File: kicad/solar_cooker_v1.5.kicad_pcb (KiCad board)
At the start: 2 copper layers, 160.5 x 77.2 mm, 20 parts, among them J1 Pt100, J2 microSD, J3 clock_module, J4 Pt100, J5 BME680, J6 GPS, J7 Pt100, J8 display, U1 anemometer, U2 AM2315C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

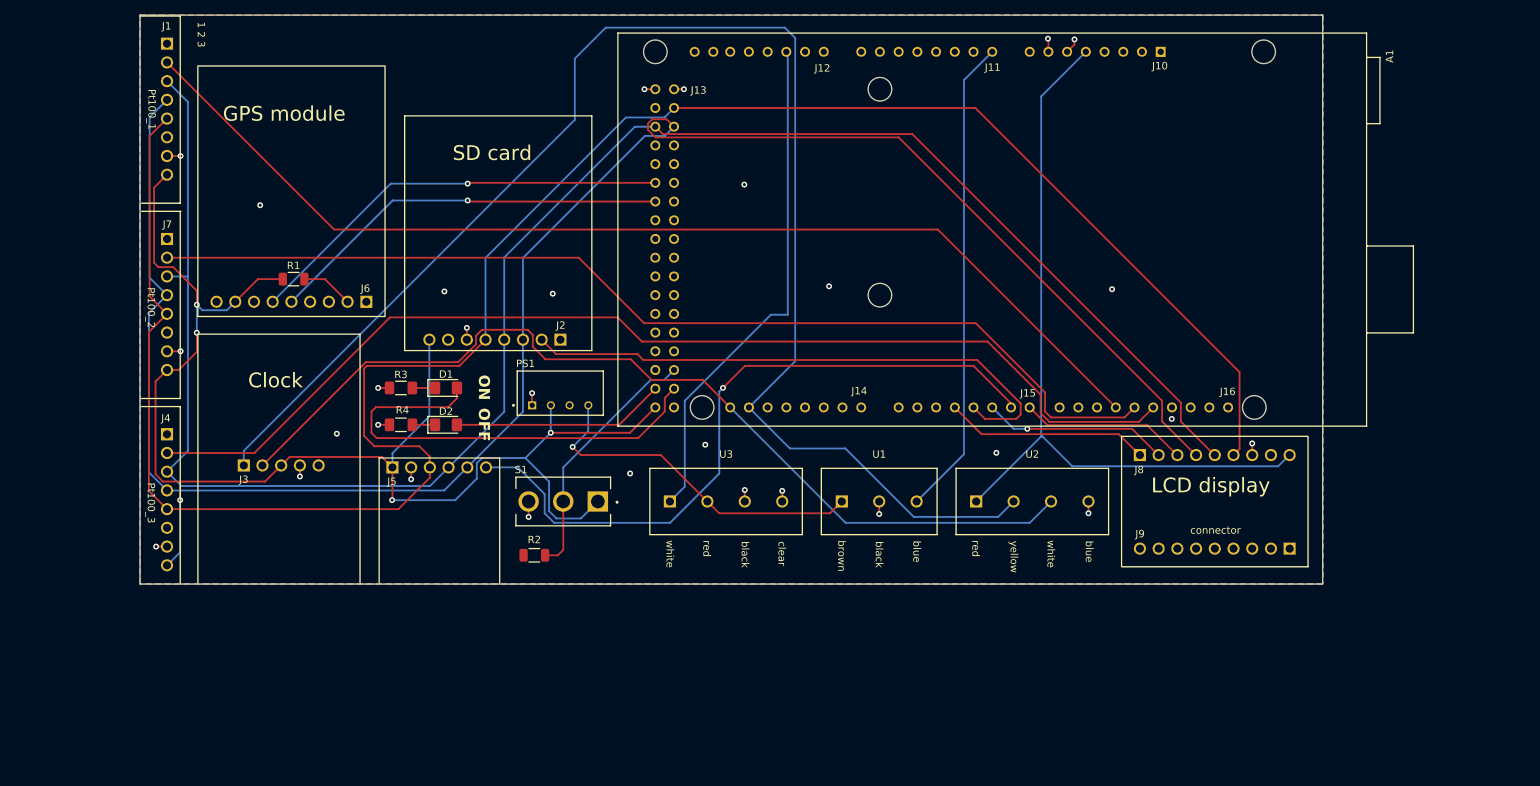
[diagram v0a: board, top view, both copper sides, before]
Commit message: fixed GPS and clock module in kicad
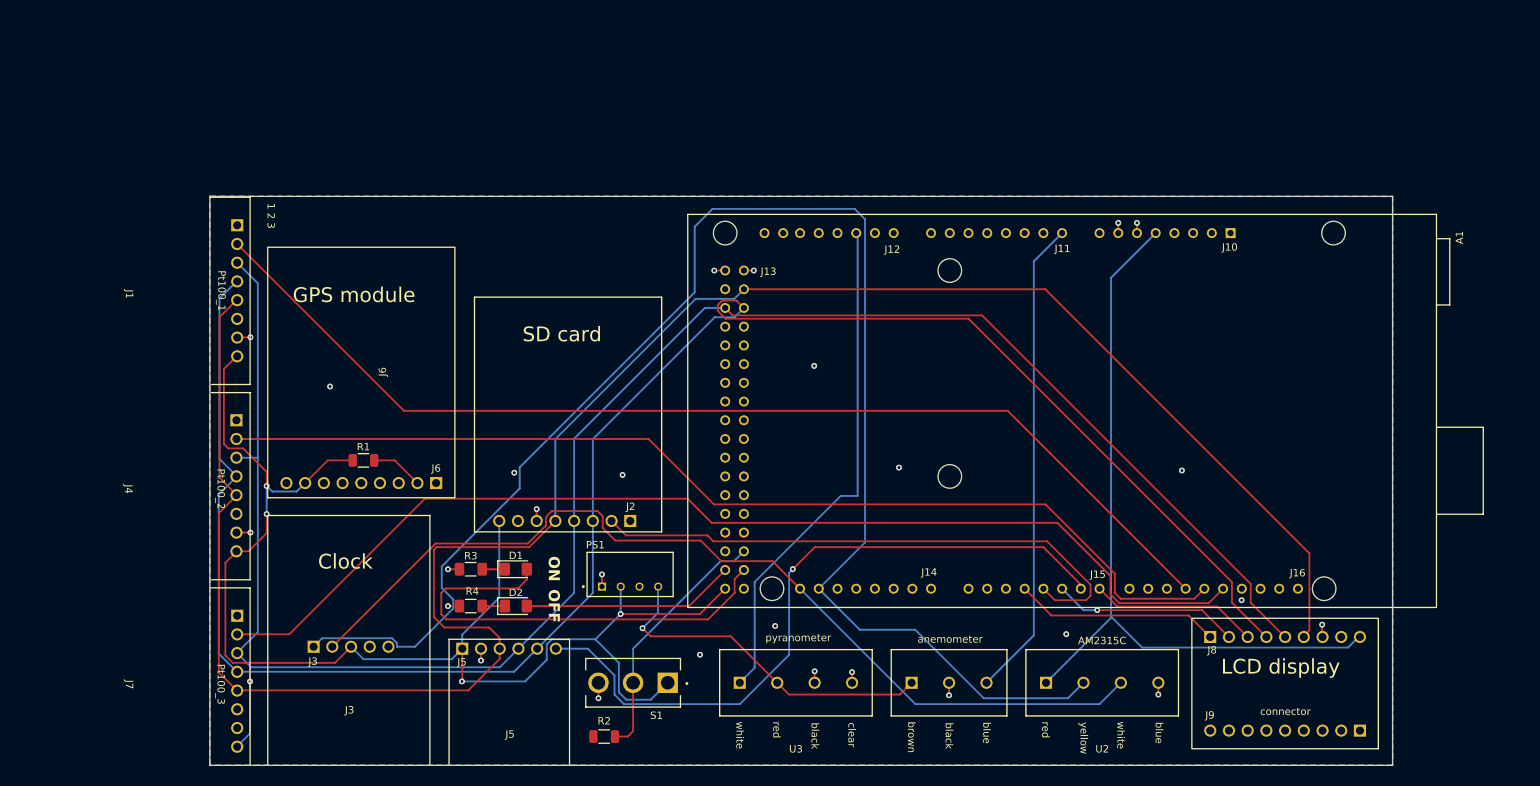
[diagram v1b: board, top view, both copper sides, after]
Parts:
- D1: value LED -> LED_GREEN
- D2: value LED -> LED_RED
- J1, J4, J7: footprint custom_components:Pt100 -> custom_components:PT100
- R1, R2: value R_Small -> 10k
- R3, R4: value R_Small -> 150
- moved J7 52.0 mm to (57.8, 145.8)
- moved J8 26.5 mm to (216.0, 144.9)
- moved J1 26.4 mm to (57.8, 92.9)
- moved R2 26.4 mm to (123.6, 153.3)
- moved D2 26.4 mm to (111.6, 135.6)
- moved J2 26.4 mm to (118.7, 107.7)
- moved J3 26.4 mm to (89.3, 141.0)
- moved J6 26.4 mm to (90.6, 103.9)
- moved PS1 26.4 mm to (127.1, 131.3)
- moved R4 26.4 mm to (105.5, 135.6)
- moved A1 26.4 mm to (185.7, 109.1)
- moved U1 26.4 mm to (170.4, 146.0)
- moved U2 26.4 mm to (191.2, 146.0)
- moved U3 26.4 mm to (149.6, 146.0)
- moved D1 26.4 mm to (111.6, 130.6)
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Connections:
- A1 pad 18: unconnected-(A1-Pad18) -> /TX1
- A1 pad 19: unconnected-(A1-Pad19) -> /RX1
- J4 pad 2: /D13 -> /D12
- J6 pad 5: /D43 -> /RX1
- J6 pad 6: /D45 -> /TX1
- J7 pad 2: /D12 -> /D13
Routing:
- net /D45: track 58.6 -> 0.00 mm, vias 1 -> 0
- net /D43: track 55.1 -> 0.00 mm, vias 1 -> 0
- net /SDA: track 201.7 -> 209.4 mm
- net GND: track 31.3 -> 27.2 mm, vias 30 -> 27

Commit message: footprints update
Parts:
- moved U1 21.9 mm to (192.3, 146.0)
- moved U2 19.8 mm to (171.4, 146.0)
- moved J2 9.61 mm to (117.9, 98.2)
- moved D2 8.34 mm to (115.3, 128.1)
- moved R4 7.93 mm to (107.8, 128.0), turned to 0 degrees
- moved D1 6.93 mm to (115.3, 124.7)
- moved R1 6.83 mm to (90.3, 109.0), turned to 0 degrees
- moved R3 6.31 mm to (107.8, 124.7), turned to 0 degrees
- moved A1 5.64 mm to (191.4, 108.9)
- moved R2 5.16 mm to (128.7, 154.1), turned to 180 degrees
- moved J6 4.97 mm to (90.2, 99.0)
- moved PS1 4.95 mm to (128.0, 126.4)
- moved J5 3.77 mm to (109.7, 145.8)
- moved J3 3.65 mm to (88.8, 137.4)
- moved U3 1.67 mm to (148.0, 146.0)
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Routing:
- net +5V: track 298.2 -> 0.00 mm, vias 5 -> 0
- net /SCK: track 282.9 -> 0.00 mm
- net /MISO: track 257.8 -> 0.00 mm
- net /MOSI: track 253.5 -> 0.00 mm
- net /SDA: track 209.4 -> 0.00 mm
- net /D13: track 149.6 -> 0.00 mm
- net /D11: track 148.1 -> 0.00 mm
- net /D12: track 142.4 -> 0.00 mm
- net /SCL: track 128.3 -> 0.00 mm
- net /D6: track 93.9 -> 0.00 mm, vias 1 -> 0
- net /D4: track 77.4 -> 0.00 mm
- net /A10: track 69.1 -> 0.00 mm
- net /A0: track 65.3 -> 0.00 mm
- net /D22: track 61.9 -> 0.00 mm
- net +9V: track 47.4 -> 0.00 mm, vias 1 -> 0
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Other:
- board text removed: "1 2 3"
- board text removed: "Clock"
- board text removed: "GPS module"
- board text removed: "J10"
- board text removed: "J11"
- board text removed: "J12"
- board text removed: "J13"
- board text removed: "J14"
- board text removed: "J15"
- board text removed: "J16"
- board text removed: "J9"
- board text removed: "LCD display"
- board text removed: "OFF"
- board text removed: "ON"
- board text removed: "Pt100_1"
- board text removed: "Pt100_2"
- board text removed: "Pt100_3"
- board text removed: "SD card"
- board text removed: "black"
- board text removed: "blue"
- board text removed: "brown"
- board text removed: "clear"
- board text removed: "connector"
- board text removed: "red"
- board text removed: "white"
- board text removed: "yellow"

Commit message: footprints update
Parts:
- moved J3 8.93 mm to (89.6, 146.3)
- moved J6 0.54 mm to (89.6, 99.0), turned to 0 degrees
- moved U1 0.05 mm to (192.3, 146.0)
- turned J2 to 0 degrees
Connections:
- J1 pad 1: unconnected-(J1-RDY-Pad1) -> +5V
- J1 pad 2: /D11 -> GND
- J1 pad 3: /MOSI -> unconnected-(J1-3V3-Pad3)
- J1 pad 4: /MISO -> /SCK
- J1 pad 5: /SCK -> /MISO
- J1 pad 6: unconnected-(J1-3V3-Pad6) -> /MOSI
- J1 pad 7: GND -> /D11
- J1 pad 8: +5V -> unconnected-(J1-RDY-Pad8)
- J2 pad 1: unconnected-(J2-CD-Pad1) -> +5V
- J2 pad 2: /D4 -> unconnected-(J2-3V-Pad2)
- J2 pad 3: /MISO -> GND
- J2 pad 4: /MOSI -> /SCK
- J2 pad 5: /SCK -> /MOSI
- J2 pad 6: GND -> /MISO
- J2 pad 7: unconnected-(J2-3V-Pad7) -> /D4
- J2 pad 8: +5V -> unconnected-(J2-CD-Pad8)
- J3 pad 1: /SDA -> +5V
- J3 pad 2: /SCL -> GND
- J3 pad 3: +5V -> /SCL
- J3 pad 4: GND -> /SDA
- J3 pad 5: (no net) -> unconnected-(J3-VBAT-Pad5)
- J4 pad 1: unconnected-(J4-RDY-Pad1) -> +5V
- J4 pad 2: /D12 -> GND
- J4 pad 3: /MOSI -> unconnected-(J4-3V3-Pad3)
- J4 pad 4: /MISO -> /SCK
- J4 pad 5: /SCK -> /MISO
- J4 pad 6: unconnected-(J4-3V3-Pad6) -> /MOSI
- J4 pad 7: GND -> /D12
- J4 pad 8: +5V -> unconnected-(J4-RDY-Pad8)
- J5 pad 2: GND -> unconnected-(J5-3Vo-Pad2)
- J5 pad 3: /SCK -> GND
- J5 pad 4: /MOSI -> /SCK
- J5 pad 6: /D6 -> /MOSI
- J7 pad 1: unconnected-(J7-RDY-Pad1) -> +5V
- J7 pad 2: /D13 -> GND
- J7 pad 3: /MOSI -> unconnected-(J7-3V3-Pad3)
- J7 pad 4: /MISO -> /SCK
- J7 pad 5: /SCK -> /MISO
- J7 pad 6: unconnected-(J7-3V3-Pad6) -> /MOSI
- J7 pad 7: GND -> /D13
- J7 pad 8: +5V -> unconnected-(J7-RDY-Pad8)

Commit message: all footprints ready
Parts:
- A1: moved to B.Cu
- moved R2 30.4 mm to (107.2, 132.6)
- moved S1 30.0 mm to (104.5, 125.5)
- moved R3 25.9 mm to (81.9, 123.5)
- moved R4 25.9 mm to (81.9, 126.8)
- moved D1 25.9 mm to (89.5, 123.6)
- moved D2 25.9 mm to (89.5, 127.0)
- moved A1 8.31 mm to (183.1, 108.9), turned to 90 degrees
- moved J8 8.14 mm to (208.1, 146.3)
- moved J5 7.67 mm to (117.3, 146.3)
- moved U1 6.78 mm to (185.6, 146.3)
- moved U2 6.06 mm to (165.3, 146.3)
- moved PS1 5.86 mm to (122.2, 125.5)
- moved U3 5.30 mm to (142.7, 146.3)
- moved J1 3.92 mm to (61.1, 92.1)
- moved J4 3.92 mm to (61.1, 118.6)
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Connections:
- J8 pad 1: /D3 -> +5V
- J8 pad 2: /D5 -> unconnected-(J8-Lite-Pad2)
- J8 pad 3: /D7 -> GND
- J8 pad 4: /MISO -> /SCK
- J8 pad 6: /SCK -> /MISO
- J8 pad 7: GND -> /D7
- J8 pad 8: unconnected-(J8-Lite-Pad8) -> /D5
- J8 pad 9: +5V -> /D3
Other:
- board size 160.5 x 77.2 mm -> 152.7 x 77.2 mm

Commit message: PCB routing and footprints done
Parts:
- moved R1 1.13 mm to (90.5, 110.1)
- moved R4 1.07 mm to (81.9, 127.9), turned to 180 degrees
- moved D2 0.89 mm to (89.5, 127.9)
- moved R3 0.51 mm to (81.9, 123.0), turned to 180 degrees
- moved D1 0.48 mm to (89.5, 123.1)
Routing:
- net +5V: track 0.00 -> 303.9 mm, vias 0 -> 1
- net /SCK: track 0.00 -> 257.4 mm
- net /MOSI: track 0.00 -> 237.7 mm, vias 0 -> 1
- net /MISO: track 0.00 -> 226.4 mm, vias 0 -> 3
- net /SCL: track 0.00 -> 155.6 mm, vias 0 -> 2
- net /D13: track 0.00 -> 154.5 mm
- net /D12: track 0.00 -> 142.6 mm, vias 0 -> 2
- net /SDA: track 0.00 -> 142.2 mm
- net /D11: track 0.00 -> 129.1 mm
- net /D6: track 0.00 -> 102.7 mm, vias 0 -> 1
- net /RX1: track 0.00 -> 75.3 mm
- net /TX1: track 0.00 -> 74.4 mm
- net /D22: track 0.00 -> 68.1 mm
- net /D4: track 0.00 -> 68.0 mm
- net +9V: track 0.00 -> 66.8 mm
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
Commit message: silkscreen update
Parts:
- moved R2 1.70 mm to (108.3, 131.3)
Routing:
- net GND: track 56.6 -> 34.9 mm, vias 19 -> 22
- net +5V: track 303.9 -> 310.7 mm
- net /MISO: track 226.4 -> 229.1 mm
- net /D13: track 154.5 -> 156.8 mm
- net /D6: track 102.7 -> 101.2 mm
- net /SCK: track 257.4 -> 258.5 mm
- net /D23: track 63.3 -> 64.1 mm
- net /A10: track 25.6 -> 26.3 mm
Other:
- board text added: "J10"
- board text added: "J11"
- board text added: "J12"
- board text added: "J13"
- board text added: "J14"
- board text added: "J15"
- board text added: "J16"
- board text added: "J9"
- board text added: "solar cooker testing station v2"
- board text removed: "solar cooker testing station v1"

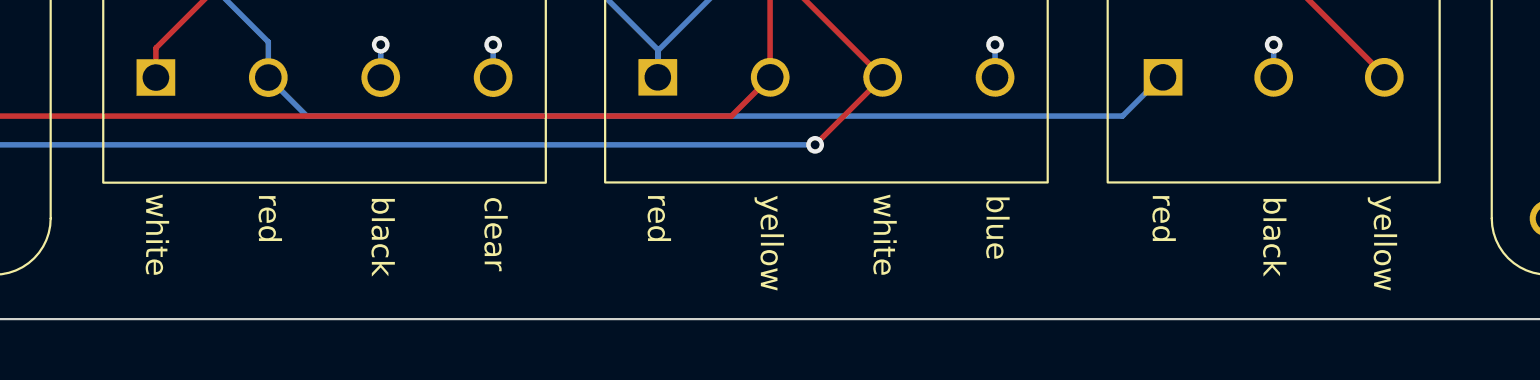
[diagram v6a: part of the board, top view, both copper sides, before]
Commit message: structure improvement kicad + added connectors
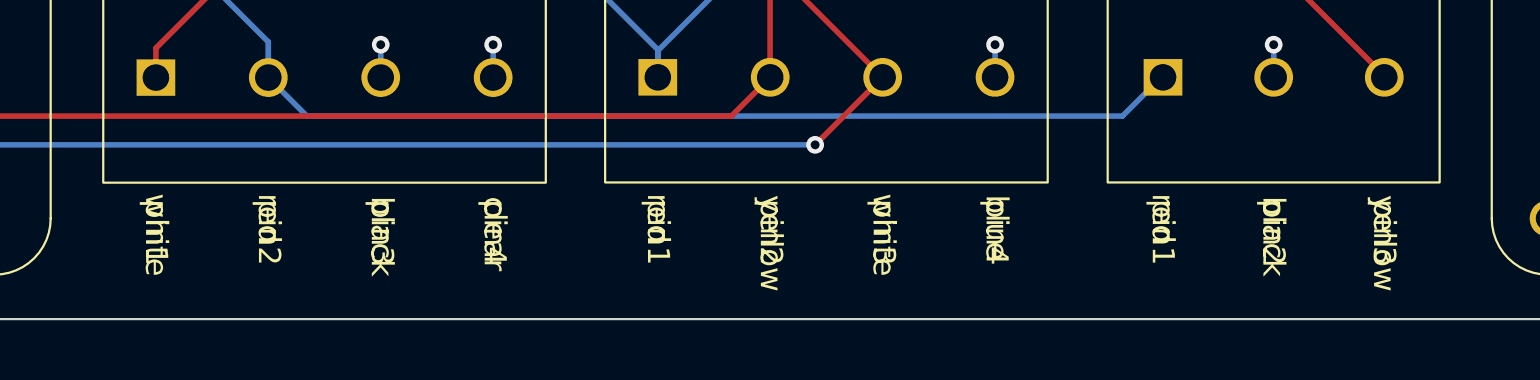
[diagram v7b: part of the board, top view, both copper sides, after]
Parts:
- J1, J4, J7: footprint custom_components:PT100 -> custom_components:Pt100
- J3: footprint custom_components:clockModule -> custom_components:clock_module

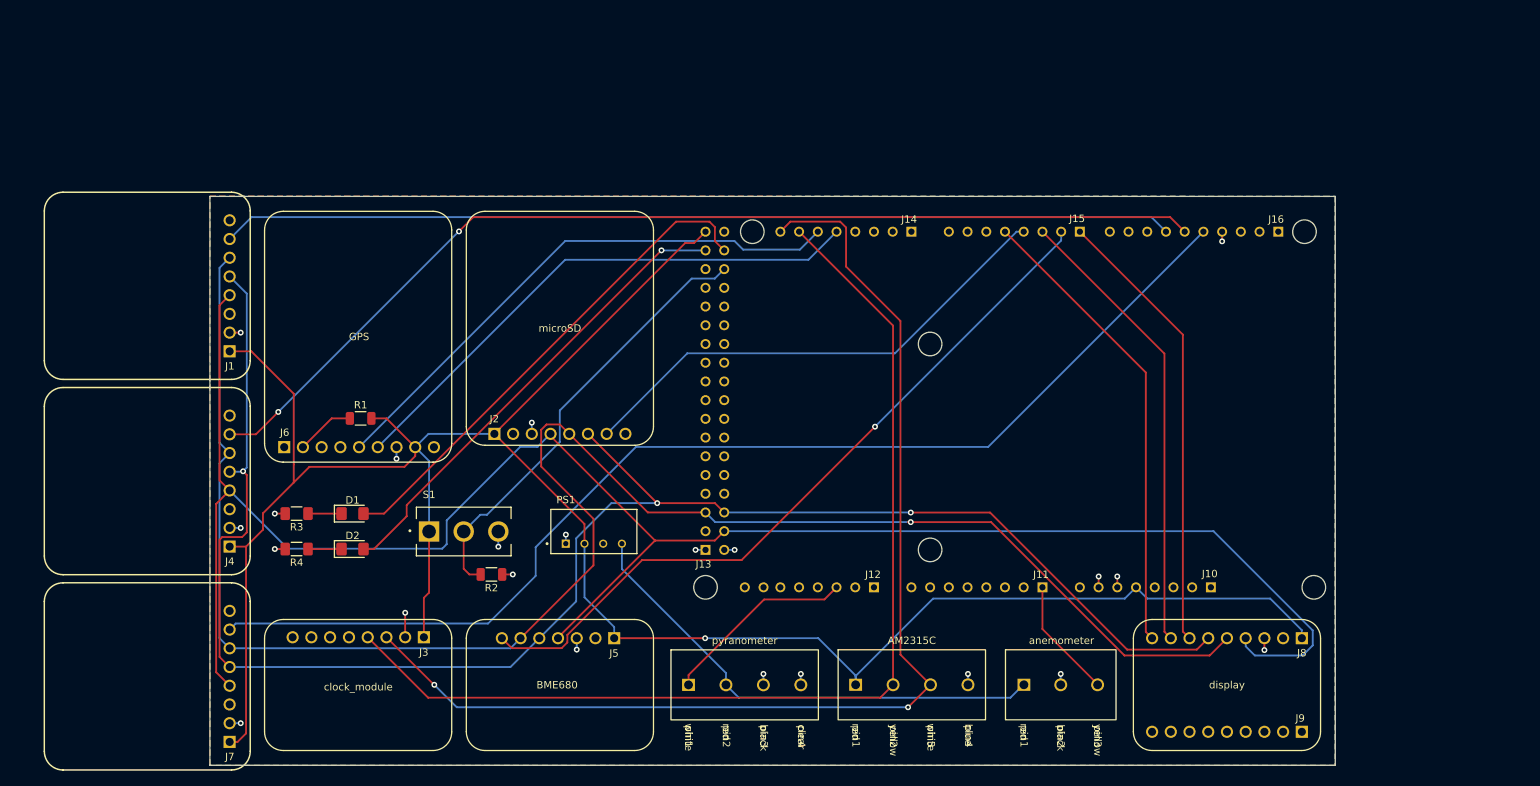
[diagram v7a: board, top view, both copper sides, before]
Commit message: bom generation from schematic
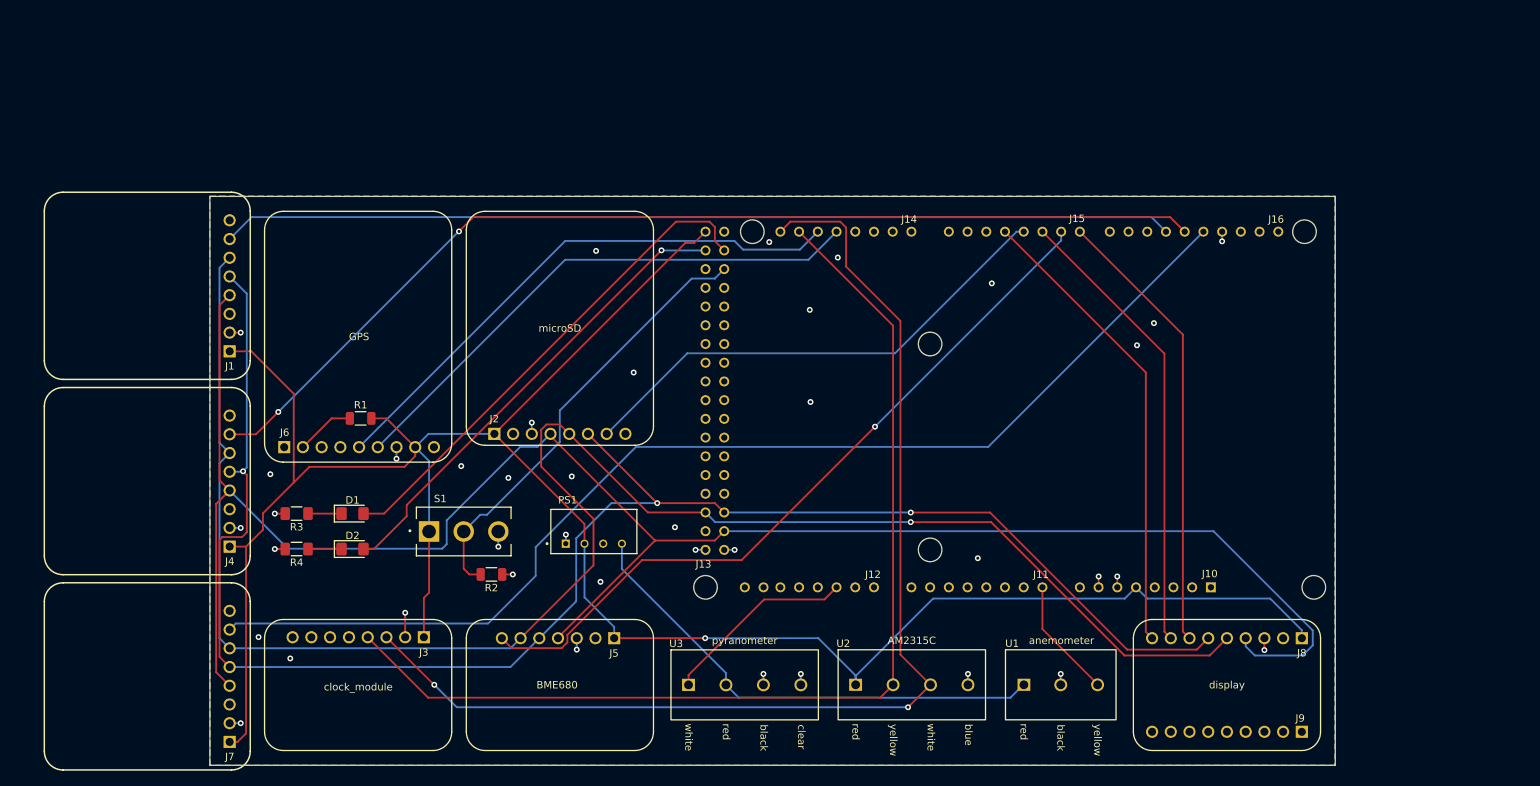
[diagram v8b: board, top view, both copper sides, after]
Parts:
- A1: footprint Arduino Mega:ARDUINO_A000067 -> A000067:ARDUINO_A000067
- PS1: footprint dcdc convertor:CONV_TBA_1-0519 -> TBA_1-0519:CONV_TBA_1-0519
- S1: footprint switch:SW_500SSP1S2M2QEA -> 500SSP1S2M2QEA:SW_500SSP1S2M2QEA
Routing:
- net GND: vias 22 -> 40
